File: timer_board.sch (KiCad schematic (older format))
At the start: 54 parts, among them CON1 AVR-ISP-6, IC1 ATMEGA32U4, K1 T9AS5D22-5, P1 USBMICRO, P2 OUT_INV, P3 Trigger, P4 OUT, Q1 NPN, Q2 NPN, U1 DS3231N, U2 74HC04, Y1 RESONATORSMD

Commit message: Added proper package for RTC and inverter
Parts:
- removed U1: DS3231N, symbol DS3231N
- added U1: DS3231MZ, ~, symbol DS3231MZ
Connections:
- wire segments 170 -> 168
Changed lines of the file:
@@
-EESchema Schematic File Version 2  date 7/4/2013 12:23:53 AM
+EESchema Schematic File Version 2  date 7/7/2013 8:03:42 PM
 LIBS:power
 LIBS:device
@@
 Sheet 1 1
 Title "Timer Board"
-Date "4 jul 2013"
+Date "8 jul 2013"
 Rev "1"
 Comp "Visgence Inc."
@@
 Text GLabel 9450 3025 0    47   Input ~ 0
 reset
-$Comp
-L DS3231N U1
-U 1 1 51C67CD3
-P 2400 1900
-F 0 "U1" H 2700 2450 60  0000 C CNN
-F 1 "DS3231N" H 2100 1500 60  0000 C CNN
-F 2 "" H 2400 1900 60  0000 C CNN
-F 3 "" H 2400 1900 60  0000 C CNN
-	1    2400 1900
-	1    0    0    -1
-$EndComp
 $Comp
 L GND #PWR04
@@
 Wire Wire Line
 	9625 3000 9875 3000
-Connection ~ 3300 2050
-Wire Wire Line
-	3300 1950 3300 2900
-Connection ~ 3300 2150
-Connection ~ 3300 2250
-Wire Wire Line
-	2600 2750 3300 2750
-Connection ~ 3300 2350
-Connection ~ 2800 2750
-Connection ~ 2700 2750
-Connection ~ 3300 2750
 Wire Wire Line
 	1350 1775 1350 1700
@@
 Wire Wire Line
 	5600 2200 5600 2100
+$Comp
+L DS3231MZ U1
+U 1 1 51DA1E27
+P 2400 1900
+F 0 "U1" H 2700 2450 60  0000 C CNN
+F 1 "DS3231MZ" H 2100 1500 60  0000 C CNN
+F 2 "~" H 2400 1900 60  0000 C CNN
+F 3 "~" H 2400 1900 60  0000 C CNN
+	1    2400 1900
+	1    0    0    -1
+$EndComp
 $EndSCHEMATC

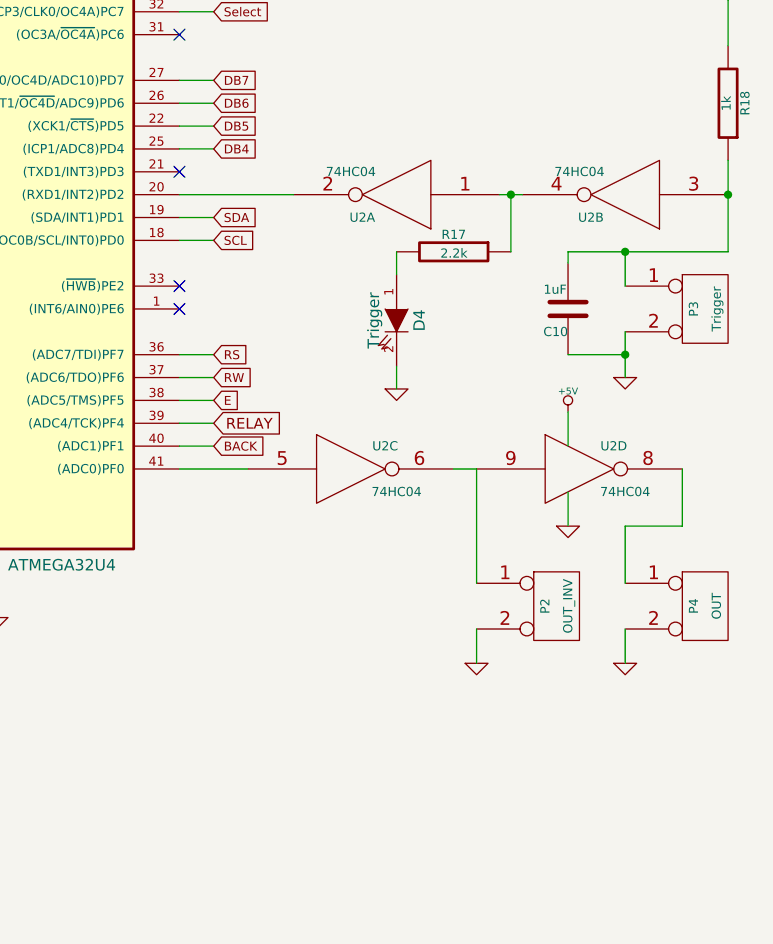
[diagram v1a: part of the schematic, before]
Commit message: Moved resistors arround
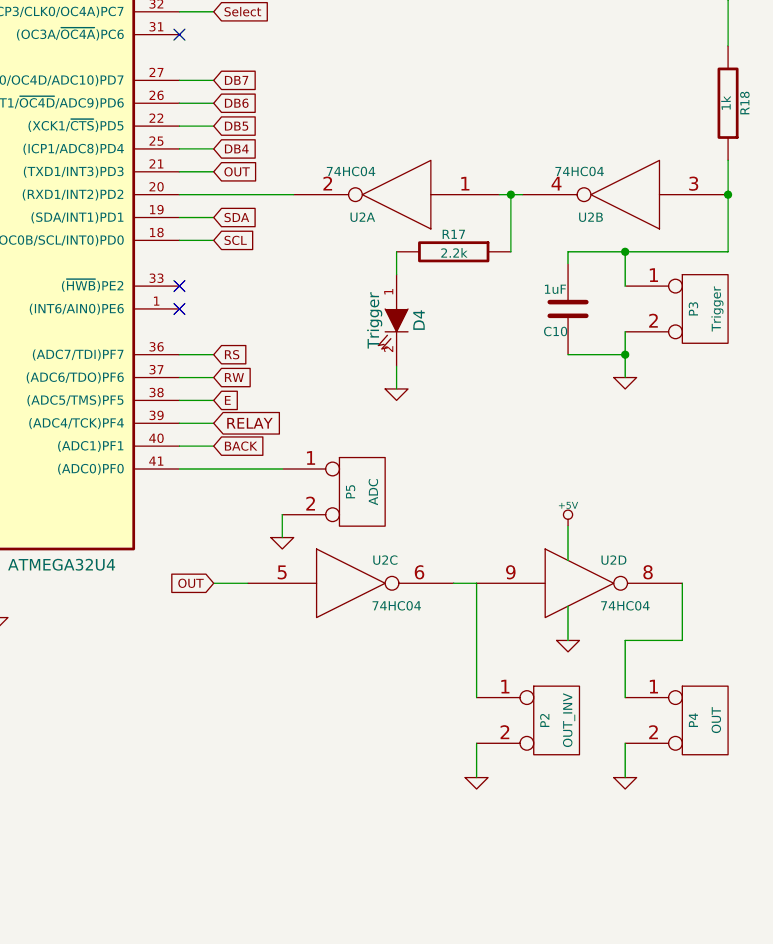
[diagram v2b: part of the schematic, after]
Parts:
- added P5: ADC, symbol CONN_2
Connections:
- net labels added: OUT
- wire segments 168 -> 171
- no-connect marks 13 -> 12
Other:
- moved on the sheet: P2, P4, U2C, U2D
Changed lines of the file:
@@
-EESchema Schematic File Version 2  date 7/7/2013 8:03:42 PM
+EESchema Schematic File Version 2  date 7/8/2013 8:19:18 PM
 LIBS:power
 LIBS:device
@@
 Sheet 1 1
 Title "Timer Board"
-Date "8 jul 2013"
+Date "9 jul 2013"
 Rev "1"
 Comp "Visgence Inc."
@@
 Comment4 ""
 $EndDescr
-$Comp
-L ATMEGA32U4 IC1
-U 1 1 51C523F1
-P 7700 3900
-F 0 "IC1" H 6900 5730 50  0000 L BNN
-F 1 "ATMEGA32U4" H 7950 2000 50  0000 L BNN
-F 2 "TQFP44" H 8200 1925 50  0001 C CNN
-F 3 "" H 7700 3900 60  0000 C CNN
-	1    7700 3900
-	1    0    0    -1
-$EndComp
 $Comp
 L RESONATORSMD Y1
@@
 L 74HC04 U2
 U 3 1 51D50B86
-P 9450 5350
-F 0 "U2" H 9600 5450 40  0000 C CNN
-F 1 "74HC04" H 9650 5250 40  0000 C CNN
-F 2 "~" H 9450 5350 60  0000 C CNN
-F 3 "~" H 9450 5350 60  0000 C CNN
-	3    9450 5350
+P 9450 5850
+F 0 "U2" H 9600 5950 40  0000 C CNN
+F 1 "74HC04" H 9650 5750 40  0000 C CNN
+F 2 "~" H 9450 5850 60  0000 C CNN
+F 3 "~" H 9450 5850 60  0000 C CNN
+	3    9450 5850
 	1    0    0    -1
 $EndComp
@@
 L CONN_2 P2
 U 1 1 51D50D20
-P 10350 5950
-F 0 "P2" V 10300 5950 40  0000 C CNN
-F 1 "OUT_INV" V 10400 5950 40  0000 C CNN
-F 2 "" H 10350 5950 60  0000 C CNN
-F 3 "" H 10350 5950 60  0000 C CNN
-	1    10350 5950
+P 10350 6450
+F 0 "P2" V 10300 6450 40  0000 C CNN
+F 1 "OUT_INV" V 10400 6450 40  0000 C CNN
+F 2 "" H 10350 6450 60  0000 C CNN
+F 3 "" H 10350 6450 60  0000 C CNN
+	1    10350 6450
 	1    0    0    -1
 $EndComp
@@
 L CONN_2 P4
 U 1 1 51D50D2D
-P 11000 5950
-F 0 "P4" V 10950 5950 40  0000 C CNN
-F 1 "OUT" V 11050 5950 40  0000 C CNN
-F 2 "" H 11000 5950 60  0000 C CNN
-F 3 "" H 11000 5950 60  0000 C CNN
-	1    11000 5950
+P 11000 6450
+F 0 "P4" V 10950 6450 40  0000 C CNN
+F 1 "OUT" V 11050 6450 40  0000 C CNN
+F 2 "" H 11000 6450 60  0000 C CNN
+F 3 "" H 11000 6450 60  0000 C CNN
+	1    11000 6450
 	1    0    0    -1
 $EndComp
@@
 L GND #PWR026
 U 1 1 51D50EA9
-P 10000 6200
-F 0 "#PWR026" H 10000 6200 30  0001 C CNN
-F 1 "GND" H 10000 6130 30  0001 C CNN
-F 2 "" H 10000 6200 60  0000 C CNN
-F 3 "" H 10000 6200 60  0000 C CNN
-	1    10000 6200
+P 10000 6700
+F 0 "#PWR026" H 10000 6700 30  0001 C CNN
+F 1 "GND" H 10000 6630 30  0001 C CNN
+F 2 "" H 10000 6700 60  0000 C CNN
+F 3 "" H 10000 6700 60  0000 C CNN
+	1    10000 6700
 	1    0    0    -1
 $EndComp
@@
 L GND #PWR027
 U 1 1 51D50EAF
-P 10650 6200
-F 0 "#PWR027" H 10650 6200 30  0001 C CNN
-F 1 "GND" H 10650 6130 30  0001 C CNN
-F 2 "" H 10650 6200 60  0000 C CNN
-F 3 "" H 10650 6200 60  0000 C CNN
-	1    10650 6200
+P 10650 6700
+F 0 "#PWR027" H 10650 6700 30  0001 C CNN
+F 1 "GND" H 10650 6630 30  0001 C CNN
+F 2 "" H 10650 6700 60  0000 C CNN
+F 3 "" H 10650 6700 60  0000 C CNN
+	1    10650 6700
 	1    0    0    -1
 $EndComp
@@
 	11100 3300 11100 3500
 Wire Wire Line
-	9000 5350 8700 5350
-Wire Wire Line
-	10000 5350 9900 5350
-Wire Wire Line
-	10000 5350 10000 5850
-Wire Wire Line
-	10900 5350 10900 5600
-Wire Wire Line
-	10900 5600 10650 5600
-Wire Wire Line
-	10650 5600 10650 5850
-Wire Wire Line
-	10000 6050 10000 6200
-Wire Wire Line
-	10650 6050 10650 6200
+	10000 5850 9900 5850
+Wire Wire Line
+	10000 5850 10000 6350
+Wire Wire Line
+	10900 5850 10900 6100
+Wire Wire Line
+	10900 6100 10650 6100
+Wire Wire Line
+	10650 6100 10650 6350
+Wire Wire Line
+	10000 6550 10000 6700
+Wire Wire Line
+	10650 6550 10650 6700
 Connection ~ 2250 7150
 Connection ~ 2900 7150
@@
 L 74HC04 U2
 U 4 1 51D51E37
-P 10450 5350
-F 0 "U2" H 10600 5450 40  0000 C CNN
-F 1 "74HC04" H 10650 5250 40  0000 C CNN
-F 2 "~" H 10450 5350 60  0000 C CNN
-F 3 "~" H 10450 5350 60  0000 C CNN
-	4    10450 5350
+P 10450 5850
+F 0 "U2" H 10600 5950 40  0000 C CNN
+F 1 "74HC04" H 10650 5750 40  0000 C CNN
+F 2 "~" H 10450 5850 60  0000 C CNN
+F 3 "~" H 10450 5850 60  0000 C CNN
+	4    10450 5850
 	1    0    0    -1
 $EndComp
@@
 L +5V #PWR036
 U 1 1 51D52028
-P 10400 5100
-F 0 "#PWR036" H 10400 5190 20  0001 C CNN
-F 1 "+5V" H 10400 5190 30  0000 C CNN
-F 2 "" H 10400 5100 60  0000 C CNN
-F 3 "" H 10400 5100 60  0000 C CNN
-	1    10400 5100
-	1    0    0    -1
-$EndComp
-$Comp
-L GND #PWR037
-U 1 1 51D521DA
 P 10400 5600
-F 0 "#PWR037" H 10400 5600 30  0001 C CNN
-F 1 "GND" H 10400 5530 30  0001 C CNN
+F 0 "#PWR036" H 10400 5690 20  0001 C CNN
+F 1 "+5V" H 10400 5690 30  0000 C CNN
 F 2 "" H 10400 5600 60  0000 C CNN
 F 3 "" H 10400 5600 60  0000 C CNN
 	1    10400 5600
+	1    0    0    -1
+$EndComp
+$Comp
+L GND #PWR037
+U 1 1 51D521DA
+P 10400 6100
+F 0 "#PWR037" H 10400 6100 30  0001 C CNN
+F 1 "GND" H 10400 6030 30  0001 C CNN
+F 2 "" H 10400 6100 60  0000 C CNN
+F 3 "" H 10400 6100 60  0000 C CNN
+	1    10400 6100
 	1    0    0    -1
 $EndComp
@@
 	6000 3000 6000 2600
 Wire Wire Line
-	10400 5100 10400 5250
-Wire Wire Line
-	10400 5600 10400 5450
-NoConn ~ 8700 4050
+	10400 5600 10400 5750
+Wire Wire Line
+	10400 6100 10400 5950
 Wire Wire Line
 	5600 2200 5600 2100
@@
 	1    0    0    -1
 $EndComp
+$Comp
+L ATMEGA32U4 IC1
+U 1 1 51C523F1
+P 7700 3900
+F 0 "IC1" H 6900 5730 50  0000 L BNN
+F 1 "ATMEGA32U4" H 7950 2000 50  0000 L BNN
+F 2 "TQFP44" H 8200 1925 50  0001 C CNN
+F 3 "" H 7700 3900 60  0000 C CNN
+	1    7700 3900
+	1    0    0    -1
+$EndComp
+Text GLabel 8850 4050 2    39   Input ~ 0
+OUT
+Wire Wire Line
+	8850 4050 8700 4050
+Text GLabel 8850 5850 0    39   Input ~ 0
+OUT
+Wire Wire Line
+	8850 5850 9000 5850
+$Comp
+L CONN_2 P5
+U 1 1 51DB7417
+P 9500 5450
+F 0 "P5" V 9450 5450 40  0000 C CNN
+F 1 "ADC" V 9550 5450 40  0000 C CNN
+F 2 "" H 9500 5450 60  0000 C CNN
+F 3 "" H 9500 5450 60  0000 C CNN
+	1    9500 5450
+	1    0    0    -1
+$EndComp
+$Comp
+L GND #PWR041
+U 1 1 51DB741D
+P 9150 5650
+F 0 "#PWR041" H 9150 5650 30  0001 C CNN
+F 1 "GND" H 9150 5580 30  0001 C CNN
+F 2 "" H 9150 5650 60  0000 C CNN
+F 3 "" H 9150 5650 60  0000 C CNN
+	1    9150 5650
+	1    0    0    -1
+$EndComp
+Wire Wire Line
+	9150 5650 9150 5550
+Wire Wire Line
+	9150 5350 8700 5350
 $EndSCHEMATC

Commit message: Modified LCD
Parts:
- DS1: value 2X16_LDC -> 2X16_LCD
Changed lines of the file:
@@
-EESchema Schematic File Version 2  date 7/8/2013 8:19:18 PM
+EESchema Schematic File Version 2
 LIBS:power
 LIBS:device
@@
 Sheet 1 1
 Title "Timer Board"
-Date "9 jul 2013"
+Date "11 jul 2013"
 Rev "1"
 Comp "Visgence Inc."
@@
 P 3450 5250
 F 0 "DS1" H 3450 4900 60  0000 C CNN
-F 1 "2X16_LDC" H 3450 5100 60  0000 C CNN
+F 1 "2X16_LCD" H 3450 5100 60  0000 C CNN
 F 2 "" H 3450 5250 60  0000 C CNN
 F 3 "" H 3450 5250 60  0000 C CNN

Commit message: Added test point for 32khz, moved parts arround
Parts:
- added P6: CONN_1, symbol CONN_1
- added R19: 10k, ~, symbol R
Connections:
- wire segments 171 -> 173
- no-connect marks 12 -> 11
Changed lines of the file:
@@
 	3700 1700 3700 1450
 Wire Wire Line
-	3475 950  3700 950
+	3475 950  3950 950
 Wire Wire Line
 	3475 800  3475 950
@@
 NoConn ~ 3200 4700
 NoConn ~ 3300 4700
-NoConn ~ 3300 1850
 NoConn ~ 8700 4650
 NoConn ~ 8700 4550
@@
 Wire Wire Line
 	9150 5350 8700 5350
+$Comp
+L R R19
+U 1 1 51DE396D
+P 3950 1200
+F 0 "R19" V 4030 1200 40  0000 C CNN
+F 1 "10k" V 3957 1201 40  0000 C CNN
+F 2 "~" V 3880 1200 30  0000 C CNN
+F 3 "~" H 3950 1200 30  0000 C CNN
+	1    3950 1200
+	1    0    0    -1
+$EndComp
+Wire Wire Line
+	3300 1850 4100 1850
+Wire Wire Line
+	3950 1850 3950 1450
+Connection ~ 3700 950
+$Comp
+L CONN_1 P6
+U 1 1 51DE3B27
+P 4250 1850
+F 0 "P6" H 4330 1850 40  0000 L CNN
+F 1 "CONN_1" H 4250 1905 30  0001 C CNN
+F 2 "" H 4250 1850 60  0000 C CNN
+F 3 "" H 4250 1850 60  0000 C CNN
+	1    4250 1850
+	1    0    0    -1
+$EndComp
+Connection ~ 3950 1850
 $EndSCHEMATC
